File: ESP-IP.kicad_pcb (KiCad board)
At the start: 4 copper layers, 50 x 25 mm, 43 parts, among them J1 Serial and power, J2 Programming Pads, J3 Comms and power, Q1 L78M05ABDT-TR, Q2 MMBT5551L, SW1 SW_Push, SW2 SW_Push, U1 ESP32-WROOM-32U, U3 TXS0102DCU, U4 AMS1117-3.3

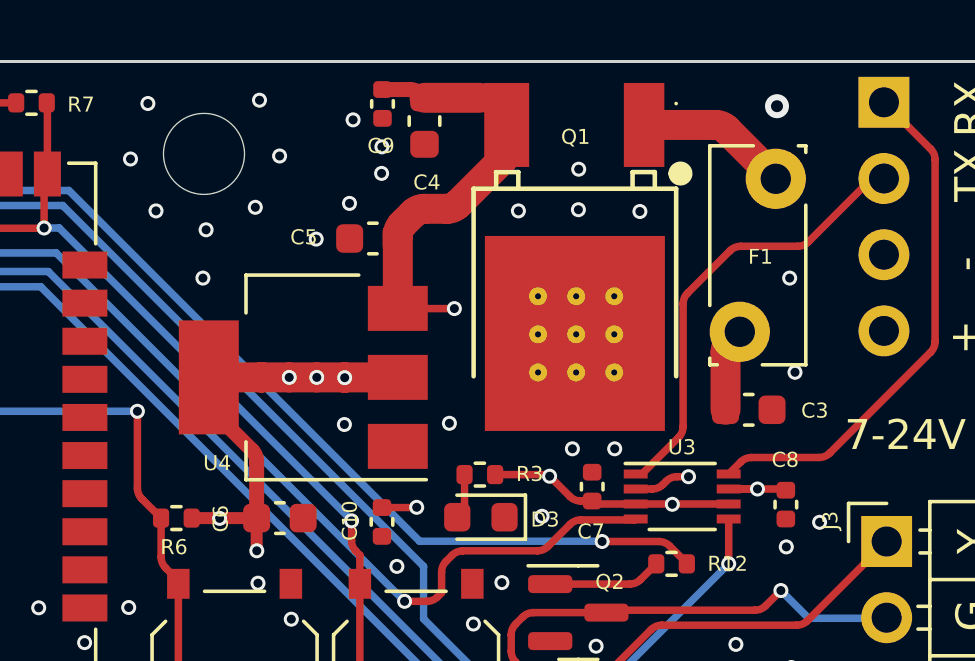
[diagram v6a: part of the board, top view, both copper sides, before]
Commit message: chore: drop some vias and refill
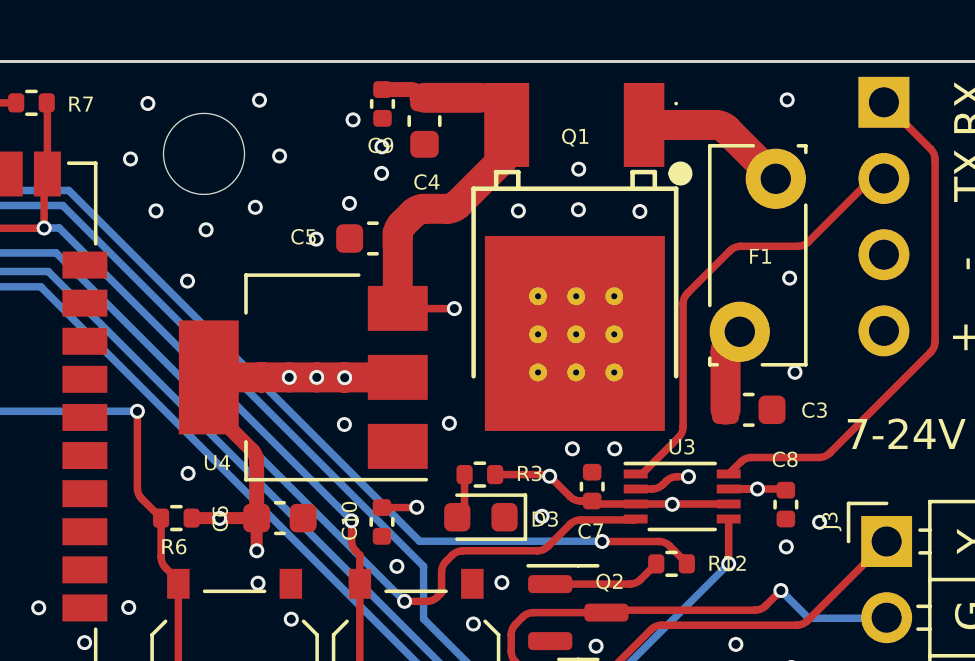
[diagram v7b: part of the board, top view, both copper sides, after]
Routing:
- net GND: vias 68 -> 69
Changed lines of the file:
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@@
   (segment (start 113.206686 113.3) (end 112.66 113.3) (width 0.25) (layer "F.Cu") (net 1))
   (segment (start 113.678316 113.03879) (end 113.565896 113.15121) (width 0.25) (layer "F.Cu") (net 1))
+  (via (at 117.71 100.33) (size 0.5) (drill 0.3) (layers "F.Cu" "B.Cu") (free) (net 1))
   (via (at 98.34 104.66) (size 0.5) (drill 0.3) (layers "F.Cu" "B.Cu") (free) (net 1))
   (via (at 96.67 104.03) (size 0.5) (drill 0.3) (layers "F.Cu" "B.Cu") (free) (net 1))
@@
   (via (at 117.792 106.27) (size 0.5) (drill 0.3) (layers "F.Cu" "B.Cu") (free) (net 1))
   (via (at 100.07 116.44) (size 0.5) (drill 0.3) (layers "F.Cu" "B.Cu") (free) (net 1))
-  (via (at 117.37 100.54) (size 0.8) (drill 0.4) (layers "F.Cu" "B.Cu") (free) (net 1))
   (via (at 103.12 103.78) (size 0.5) (drill 0.3) (layers "F.Cu" "B.Cu") (free) (net 1))
   (via (at 99.377 119.478) (size 0.5) (drill 0.3) (layers "F.Cu" "B.Cu") (free) (net 1))
@@
   (via (at 104.19 102.78) (size 0.5) (drill 0.3) (layers "F.Cu" "B.Cu") (free) (net 1))
   (via (at 116 118.48) (size 0.5) (drill 0.3) (layers "F.Cu" "B.Cu") (free) (net 1))
+  (via (at 97.74 112.78) (size 0.5) (drill 0.3) (layers "F.Cu" "B.Cu") (free) (net 1))
   (via (at 102.01 104.97) (size 0.5) (drill 0.3) (layers "F.Cu" "B.Cu") (free) (net 1))
   (via (at 114.42 112.89) (size 0.5) (drill 0.3) (layers "F.Cu" "B.Cu") (net 1))
@@
   (via (at 78.95 104.28) (size 0.5) (drill 0.3) (layers "F.Cu" "B.Cu") (free) (net 1))
   (via (at 117.97 109.41) (size 0.5) (drill 0.3) (layers "F.Cu" "B.Cu") (free) (net 1))
-  (via (at 98.234 106.27) (size 0.5) (drill 0.3) (layers "F.Cu" "B.Cu") (free) (net 1))
+  (via (at 97.72 106.37) (size 0.5) (drill 0.3) (layers "F.Cu" "B.Cu") (free) (net 1))
   (via (at 95.82 102.3) (size 0.5) (drill 0.3) (layers "F.Cu" "B.Cu") (free) (net 1))
   (via (at 76.68 117.7) (size 0.5) (drill 0.3) (layers "F.Cu" "B.Cu") (free) (net 1))
